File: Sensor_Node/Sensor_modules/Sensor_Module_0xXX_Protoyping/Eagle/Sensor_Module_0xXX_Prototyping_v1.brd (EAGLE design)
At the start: 55 x 35 mm, 36 parts, among them J1 M04_SMD_90, J4 ARDUINO_ISP, U2 ATMEGA328P_TQFP, Y1 8MHZ

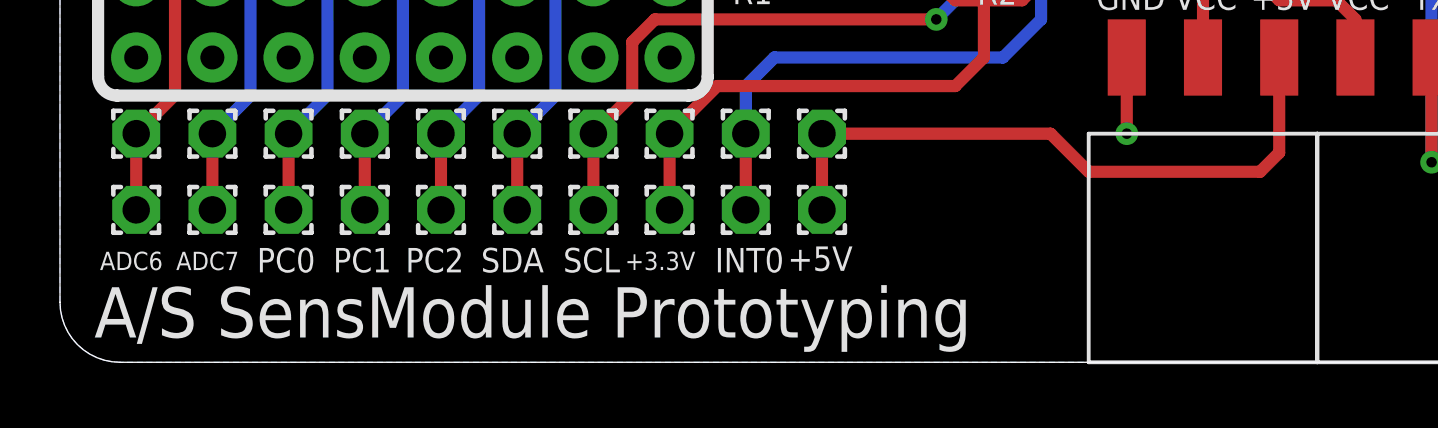
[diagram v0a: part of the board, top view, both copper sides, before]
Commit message: Renaming boards to modules inside eagle files
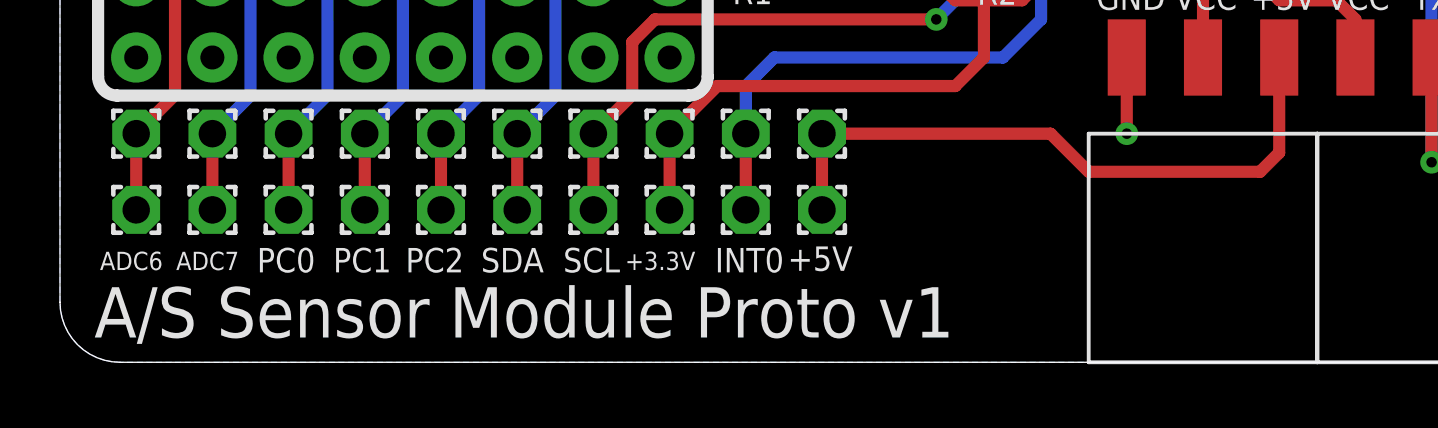
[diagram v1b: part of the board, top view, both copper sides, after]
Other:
- board text added: "A/S Sensor Module Proto v1"
- board text removed: "A/S SensModule Prototyping"
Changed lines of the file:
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@@
 <?xml version="1.0" encoding="utf-8"?>
 <!DOCTYPE eagle SYSTEM "eagle.dtd">
-<eagle version="8.4.2">
+<eagle version="9.1.1">
 <drawing>
 <settings>
@@
 <text x="47.625" y="11.7475" size="0.8128" layer="21">RX</text>
 <text x="49.8475" y="11.7475" size="0.8128" layer="21">GND</text>
-<text x="1.143" y="0.8255" size="1.6764" layer="21">A/S SensModule Prototyping</text>
+<text x="1.143" y="0.8255" size="1.6764" layer="21">A/S Sensor Module Proto v1</text>
 <text x="53.6575" y="33.9725" size="1.016" layer="21" rot="R180">FTDI</text>
 <circle x="52.07" y="31.115" radius="1.27" width="0.4064" layer="21"/>
@@
 <param name="checkRestrict" value="1"/>
 <param name="checkStop" value="0"/>
+<param name="checkValues" value="0"/>
+<param name="checkNames" value="1"/>
+<param name="checkWireStubs" value="1"/>
+<param name="checkPolygonWidth" value="0"/>
 <param name="useDiameter" value="13"/>
 <param name="maxErrors" value="50"/>
@@
 </signal>
 </signals>
+<mfgpreviewcolors>
+<mfgpreviewcolor name="soldermaskcolor" color="0xC8008000"/>
+<mfgpreviewcolor name="silkscreencolor" color="0xFFFEFEFE"/>
+<mfgpreviewcolor name="backgroundcolor" color="0xFF282828"/>
+<mfgpreviewcolor name="coppercolor" color="0xFFFFBF00"/>
+<mfgpreviewcolor name="substratecolor" color="0xFF786E46"/>
+</mfgpreviewcolors>
 </board>
 </drawing>
